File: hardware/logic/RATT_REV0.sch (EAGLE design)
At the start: 86 parts, among them J3 F-1X06-SIP-100-40, J4 F-1X07-SIP-100-40, J5 F-1X02-SIP-100-40, Q1 2.5A/30V, Q2 MBT3904DW1T1, Q3 2.5A/30V, Q5 2N7002, Q6 2.5A/30V, U3 MCP73831, U5 AP2112K-3.3V, U6 PCA9539PW

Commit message: Forgot to save first
derp
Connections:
- removed net N$40: U$1.GPIO17/GEN0
- net !I/O_RESET: now also U$1.GPIO17/GEN0
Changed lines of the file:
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@@
-</segment>
-</net>
-<net name="N$40" class="0">
-<segment>
-<pinref part="U$1" gate="G$1" pin="GPIO17/GEN0"/>
-<wire x1="101.6" y1="-81.28" x2="96.52" y2="-81.28" width="0.1524" layer="91"/>
-<label x="96.52" y="-81.28" size="1.27" layer="95" rot="R180" xref="yes"/>
 </segment>
 </net>
@@
 <label x="50.8" y="160.02" size="1.27" layer="95" rot="R180" xref="yes"/>
 </segment>
+<segment>
+<pinref part="U$1" gate="G$1" pin="GPIO17/GEN0"/>
+<wire x1="101.6" y1="-81.28" x2="96.52" y2="-81.28" width="0.1524" layer="91"/>
+<label x="96.52" y="-81.28" size="1.27" layer="95" rot="R180" xref="yes"/>
+</segment>
 </net>

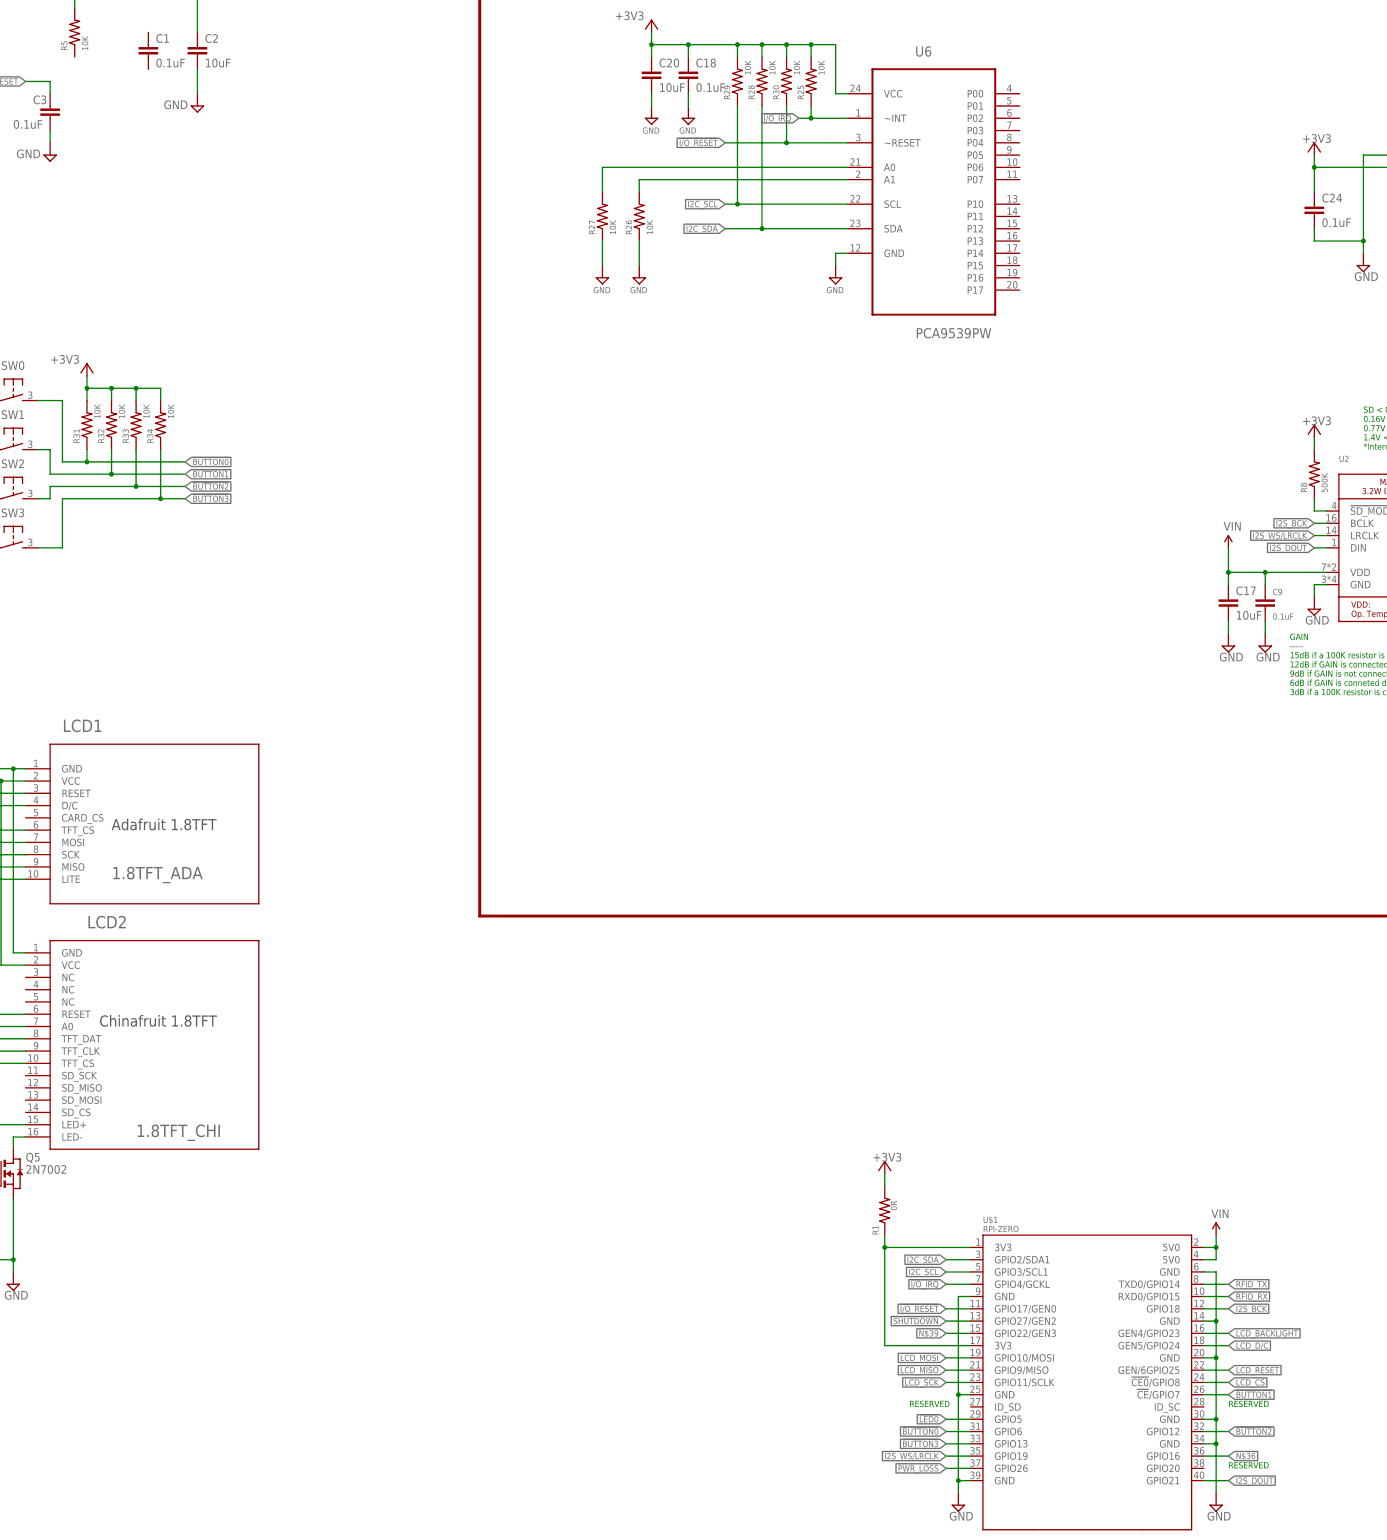
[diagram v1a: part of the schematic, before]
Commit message: new display, buttons moved
Added chinafruit 2.0, moved buttons to i/o expander, added i/o lines to expander
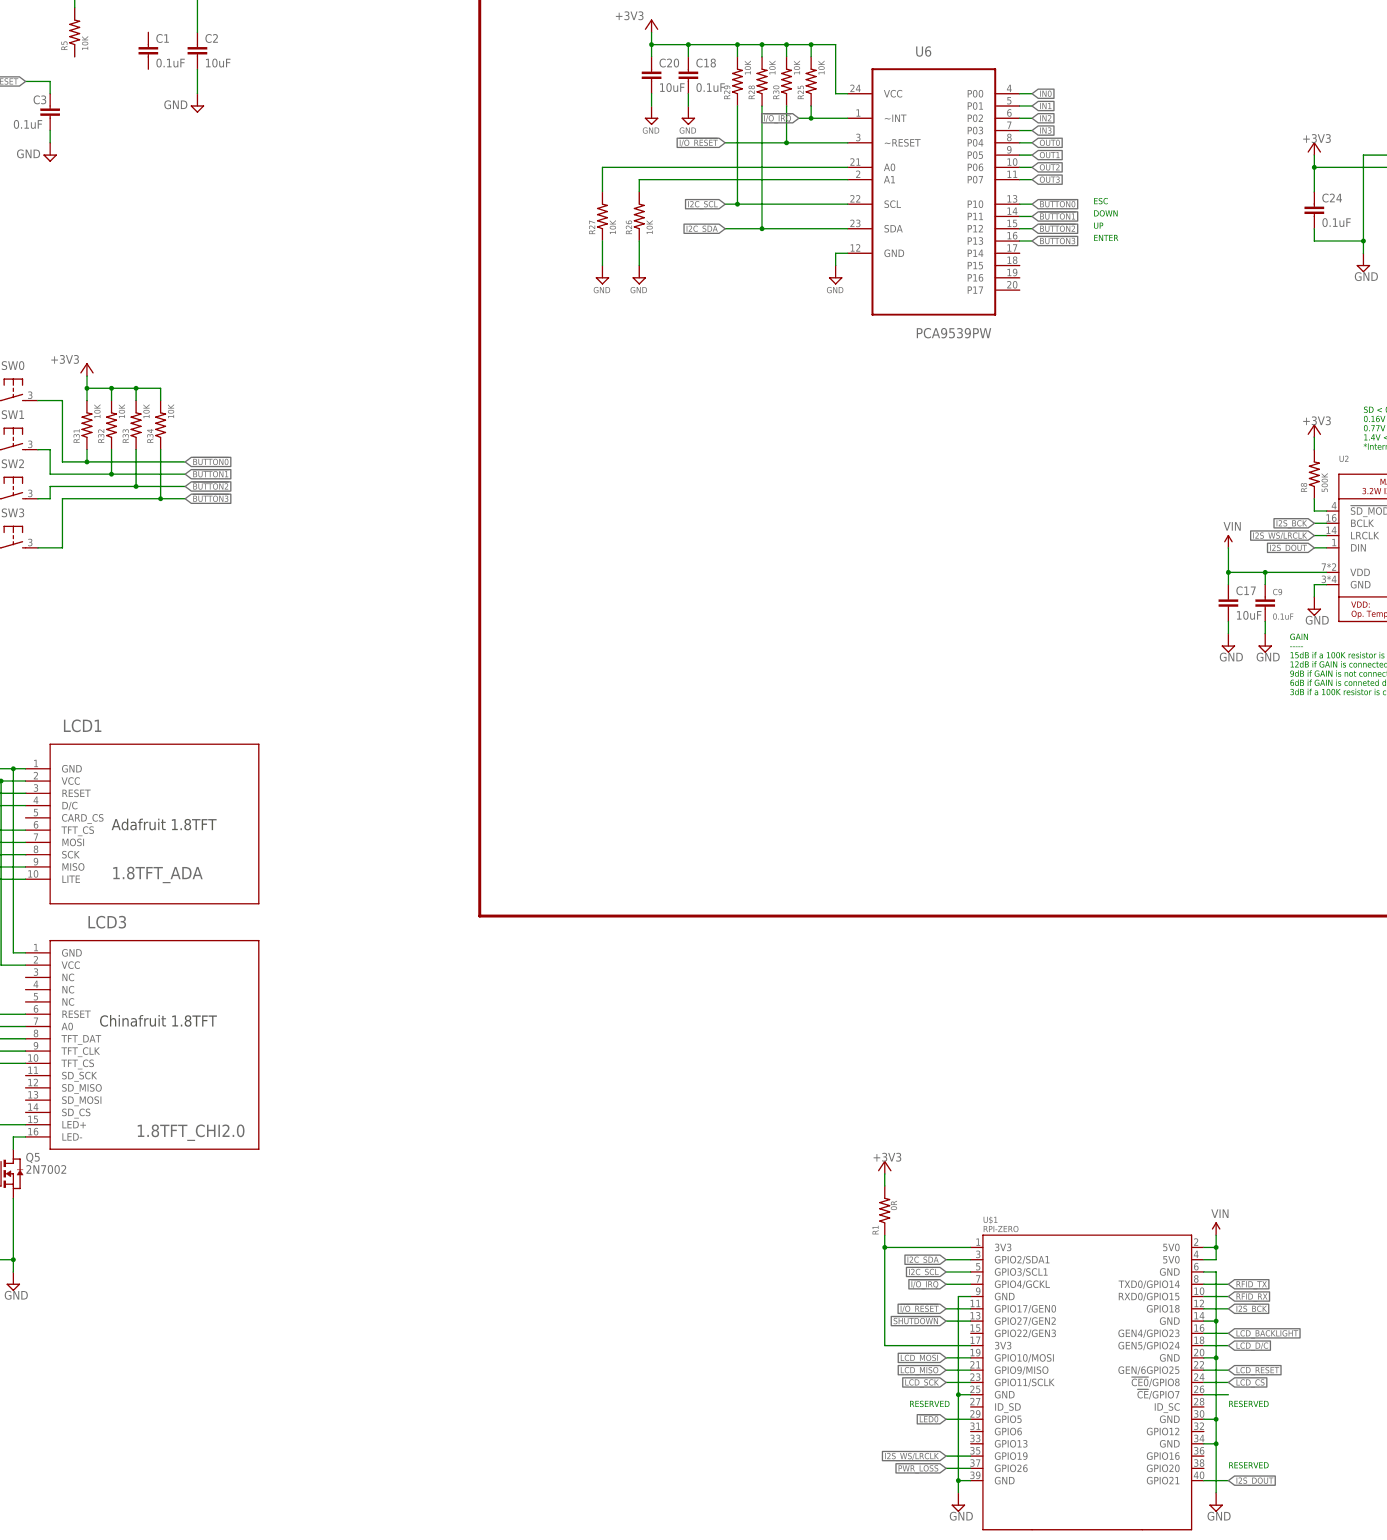
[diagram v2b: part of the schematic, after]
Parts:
- removed LCD2: 1.8TFT_CHI, MakeIt_Labs:1.8TFT_CHI
- added LCD3: 1.8TFT_CHI2.0, MakeIt_Labs:1.8TFT_CHI2.0
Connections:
- removed net N$36: U$1.GPIO16
- removed net N$39: U$1.GPIO22/GEN3
- new net IN0: U6.P00
- new net IN1: U6.P01
- new net IN2: U6.P02
- new net IN3: U6.P03
- new net N$13: U$1.!CE!/GPIO7
- new net OUT0: U6.P04
- new net OUT1: U6.P05
- new net OUT2: U6.P06
- new net OUT3: U6.P07
- net !BUTTON0: now also U6.P10; no longer U$1.GPIO6
- net !BUTTON1: now also U6.P11; no longer U$1.!CE!/GPIO7
- net !BUTTON2: now also U6.P12; no longer U$1.GPIO12
- net !BUTTON3: now also U6.P13; no longer U$1.GPIO13
- net N$26: now also LCD3.LED+, LCD3.VCC; no longer LCD2.LED+, LCD2.VCC
- net N$27: now also LCD3.RESET; no longer LCD2.RESET
- net N$28: now also LCD3.A0; no longer LCD2.A0
- net N$29: now also LCD3.TFT_CS; no longer LCD2.TFT_CS
- net N$3: now also LCD3.GND; no longer LCD2.GND
- net N$30: now also LCD3.TFT_DAT; no longer LCD2.TFT_DAT
- net N$31: now also LCD3.TFT_CLK; no longer LCD2.TFT_CLK
- net N$34: now also LCD3.LED-; no longer LCD2.LED-
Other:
- note added: "DOWN"
- note added: "ENTER"
- note added: "ESC"
- note added: "UP"
